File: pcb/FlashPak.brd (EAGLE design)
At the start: 53.3 x 58.4 mm, 18 parts, among them IC1 EPROM/FLASHROM, IC2 74LS174N, IC3 74LS138N, IC4 74LS138N, X1 EXPANSION_PORT_COCO

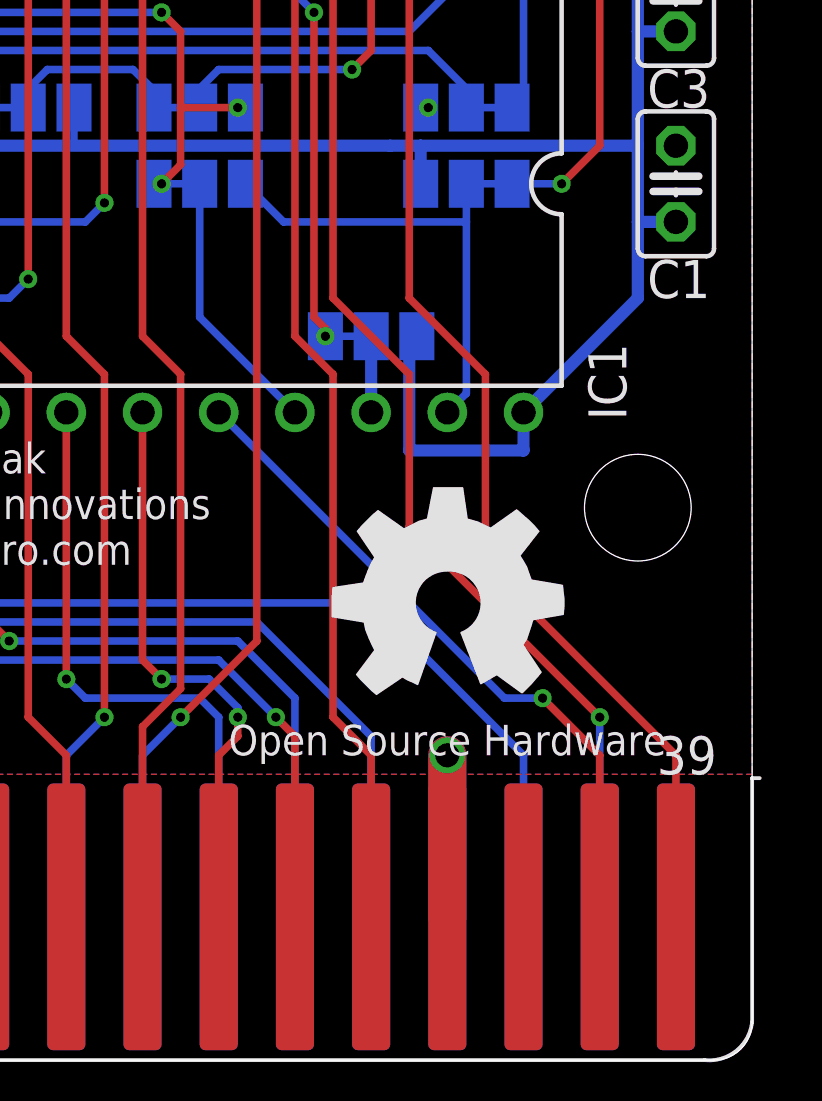
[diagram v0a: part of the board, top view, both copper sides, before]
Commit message: Fixed issue with MPI use, added ASM, and wrote sample BASIC code
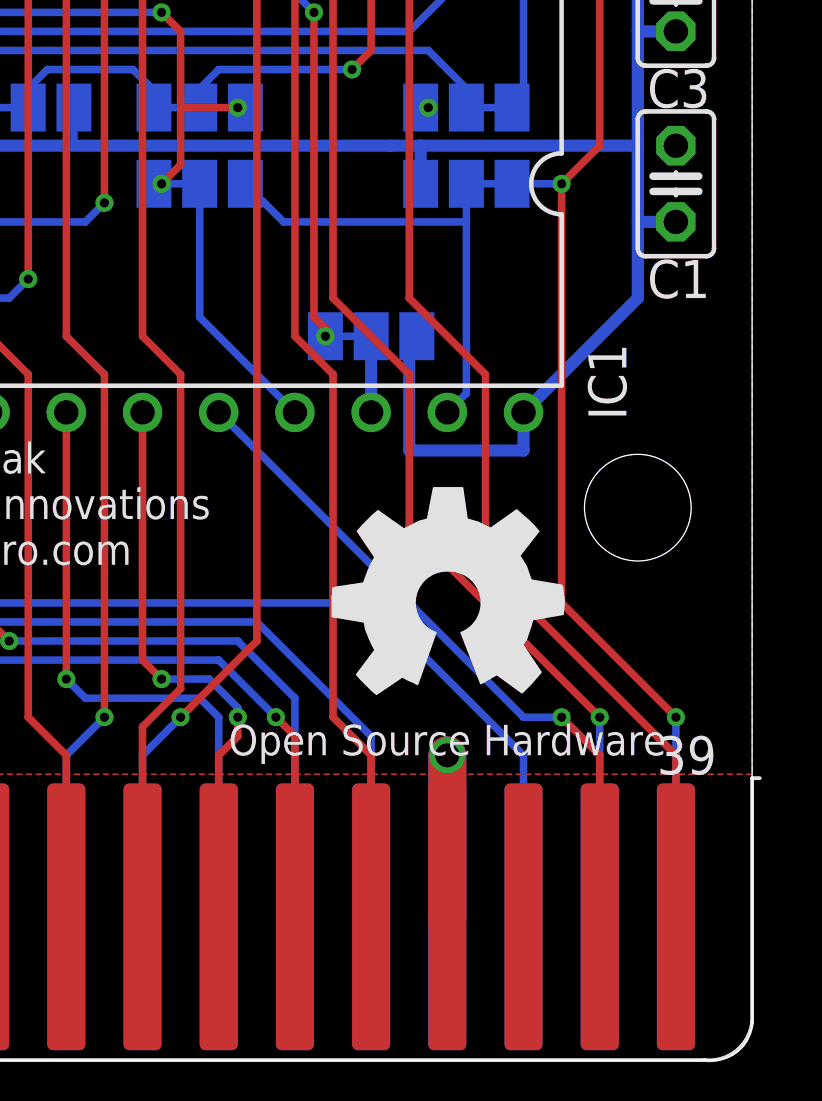
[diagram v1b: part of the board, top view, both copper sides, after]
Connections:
- removed net !SLENB: X1.40
- net !WE: now also X1.40
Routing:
- net !WE: track 29.6 -> 55.6 mm, vias 1 -> 2
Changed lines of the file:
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@@
 <contactref element="IC1" pad="28"/>
 <wire x1="21.59" y1="4.7752" x2="21.59" y2="10.16" width="0.254" layer="1"/>
-<wire x1="8.89" y1="21.59" x2="18.415" y2="12.065" width="0.254" layer="16"/>
-<wire x1="18.415" y1="12.065" x2="19.685" y2="12.065" width="0.254" layer="16"/>
-<wire x1="19.685" y1="12.065" x2="21.59" y2="10.16" width="0.254" layer="1"/>
-<via x="19.685" y="12.065" extent="1-16" drill="0.3048"/>
+<wire x1="8.89" y1="21.59" x2="19.05" y2="11.43" width="0.254" layer="16"/>
+<wire x1="19.05" y1="11.43" x2="20.32" y2="11.43" width="0.254" layer="16"/>
+<wire x1="20.32" y1="11.43" x2="21.59" y2="10.16" width="0.254" layer="1"/>
+<via x="20.32" y="11.43" extent="1-16" drill="0.3048"/>
 </signal>
 <signal name="A12">
@@
 <wire x1="-5.08" y1="40.64" x2="-5.08" y2="48.26" width="0.254" layer="1"/>
 <wire x1="-5.08" y1="48.26" x2="-6.35" y2="49.53" width="0.254" layer="1"/>
-</signal>
-<signal name="!SLENB">
-<contactref element="X1" pad="40"/>
 </signal>
 <signal name="!HALT">
@@
 <wire x1="9.779" y1="29.21" x2="11.049" y2="27.94" width="0.254" layer="16"/>
 <wire x1="11.049" y1="27.94" x2="17.145" y2="27.94" width="0.254" layer="16"/>
+<contactref element="X1" pad="40"/>
+<wire x1="24.13" y1="4.7752" x2="24.13" y2="11.43" width="0.254" layer="16"/>
+<via x="24.13" y="11.43" extent="1-16" drill="0.3048"/>
+<wire x1="24.13" y1="11.43" x2="20.32" y2="15.24" width="0.254" layer="1"/>
+<wire x1="20.32" y1="15.24" x2="20.32" y2="29.21" width="0.254" layer="1"/>
 </signal>
 <signal name="!CTS">

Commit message: Added a bit of length to the cartridge design to enable easy AUTOSTART access
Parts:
- removed AUTOSTART: (no value), jumper:JP1
- added J7: AUTOSTART, jumper:JP1
- added S1: TL36WO, switch:TL3XWO
- added SJ8: AUTOSTART, jumper-jlb:SJ
- moved GOLD_ORB_SM1 1.27 mm to (15.2, 15.2)
- renumbered 28-32 to J6
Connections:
- net !CART: now also J7.1, S1.1, SJ8.1; no longer AUTOSTART.1
- net Q: now also J7.2, S1.2, SJ8.2; no longer AUTOSTART.2
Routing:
- net !CART: track 11.5 -> 60.8 mm
- net Q: track 64.9 -> 102.3 mm
- net VCC: track 179.4 -> 174.3 mm
- net !RESET: track 37.8 -> 38.5 mm
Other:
- board size 53.3 x 58.4 mm -> 53.3 x 68.3 mm
- board text added: "28-32"
- board text removed: "FLASHPak (c)2020 RETRO Innovations www.go4retro.com"

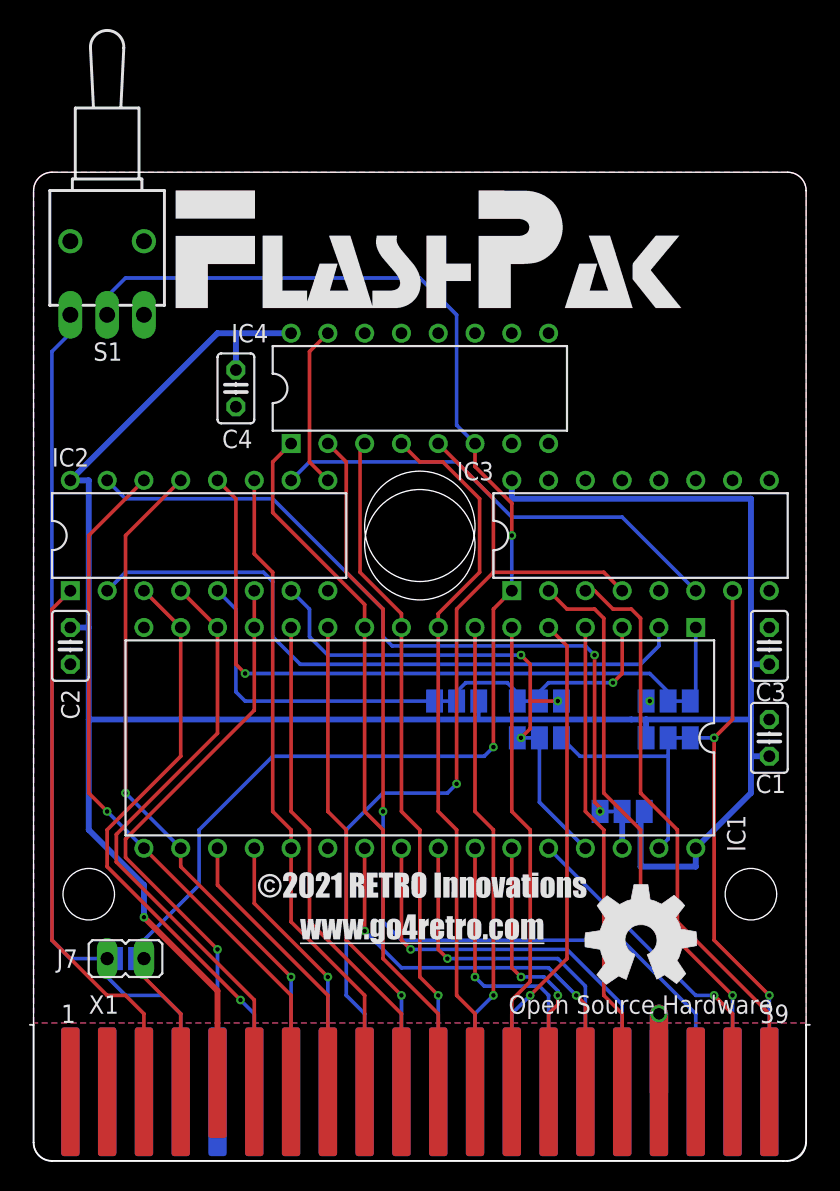
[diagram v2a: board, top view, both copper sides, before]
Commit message: Fix bug where updating bank reg while in write mod causes race condition
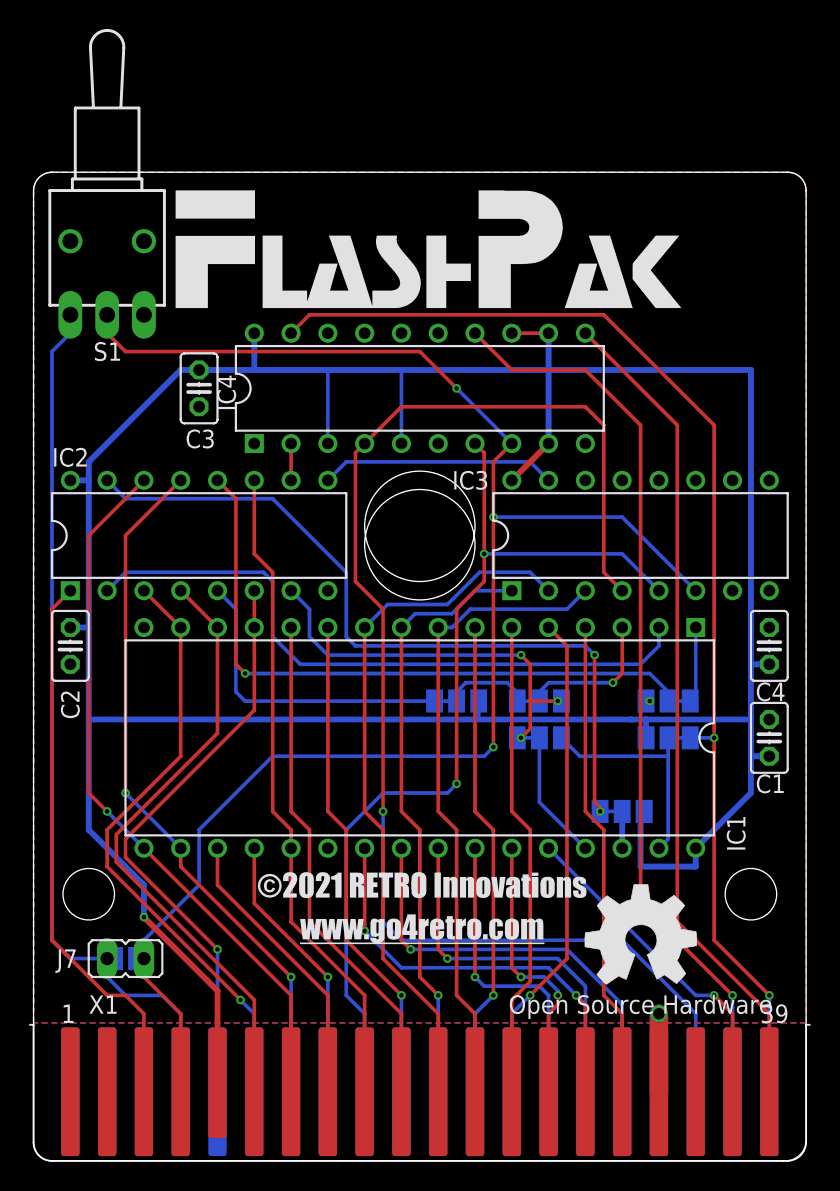
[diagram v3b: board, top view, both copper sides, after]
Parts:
- IC4: value 74LS138N -> 74LS688N; device 74xx-us-jlb:DIL16-RP -> 74xx-us-jlb:DIL20-RP
- moved C3 43.2 mm to (-15.2, 53.3), turned to 270 degrees
- moved C4 40.9 mm to (24.1, 35.6), turned to 90 degrees
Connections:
- net !LATCH: now also IC3.15; no longer IC4.15
- net !SCS: now also IC3.4, IC4.4; no longer IC4.2
- net !WE: now also IC4.19; no longer IC3.7
- net A14: now also IC4.14; no longer IC3.2
- net A15: now also IC4.11; no longer IC3.3
- net A2: now also IC3.2; no longer IC4.1
- net A3: now also IC3.1; no longer IC4.3
- net A4: now also IC3.3; no longer IC4.4
- net GND: now also IC4.1, IC4.10, IC4.15, IC4.16, IC4.17, IC4.18, IC4.6; no longer IC3.5, IC4.8
- net PGM: now also IC4.2; no longer IC3.6
- net Q: now also IC3.6, IC4.8; no longer IC3.1, IC4.6
- net R/!W: now also IC3.5, IC4.7; no longer IC3.4, IC4.5
- net VCC: now also IC4.12, IC4.13, IC4.20, IC4.3, IC4.5, IC4.9; no longer IC4.16
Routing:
- net VCC: track 174.3 -> 219.5 mm
- net !WE: track 55.6 -> 99.4 mm
- net PGM: track 32.1 -> 2.54 mm
- net !SCS: track 64.2 -> 93.7 mm
- net A14: track 41.0 -> 62.7 mm
- net A15: track 41.0 -> 57.6 mm
- net Q: track 102.3 -> 113.8 mm, vias 2 -> 3
- net A4: track 50.2 -> 44.3 mm
- net A3: track 47.1 -> 41.8 mm
- net !LATCH: track 11.2 -> 16.3 mm
- net R/!W: track 63.1 -> 65.2 mm, vias 1 -> 2
- net BA17: track 54.8 -> 56.3 mm
- net A2: track 50.0 -> 49.0 mm
- net !CART: track 60.8 -> 61.3 mm

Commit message: Vcc loop removed, final Gerbers created
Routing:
- net VCC: track 219.5 -> 185.2 mm
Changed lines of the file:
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@@
 <wire x1="14.605" y1="30.48" x2="3.81" y2="30.48" width="0.4064" layer="16"/>
 <wire x1="3.81" y1="30.48" x2="-22.86" y2="30.48" width="0.4064" layer="16"/>
-<wire x1="22.86" y1="54.61" x2="22.86" y2="34.29" width="0.4064" layer="16"/>
 <contactref element="J6" pad="3"/>
 <wire x1="24.13" y1="27.94" x2="22.86" y2="27.94" width="0.4064" layer="16"/>
@@
 <wire x1="8.89" y1="49.53" x2="8.89" y2="54.61" width="0.4064" layer="16"/>
 <wire x1="8.89" y1="57.15" x2="8.89" y2="54.61" width="0.4064" layer="16"/>
-<wire x1="22.86" y1="54.61" x2="8.89" y2="54.61" width="0.4064" layer="16"/>
 <wire x1="-6.35" y1="49.53" x2="-6.35" y2="54.61" width="0.254" layer="16"/>
 <contactref element="IC4" pad="5"/>
